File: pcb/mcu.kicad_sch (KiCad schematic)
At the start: 15 parts, among them J1 AVR-UPDI-6, U1 ATtiny1616-MNR

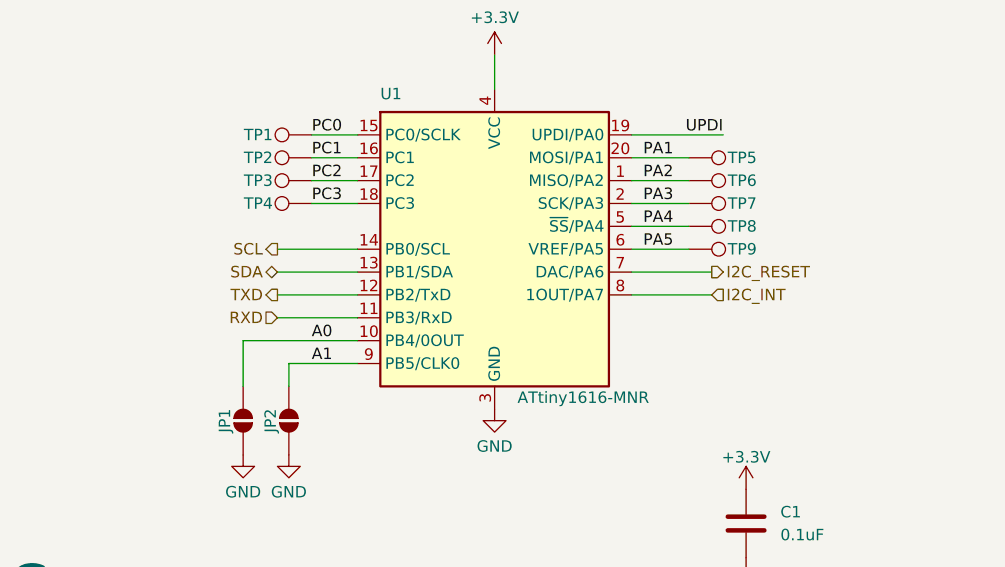
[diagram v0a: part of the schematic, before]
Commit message: Switched back to global lables
Updated all gnd and test point symbols
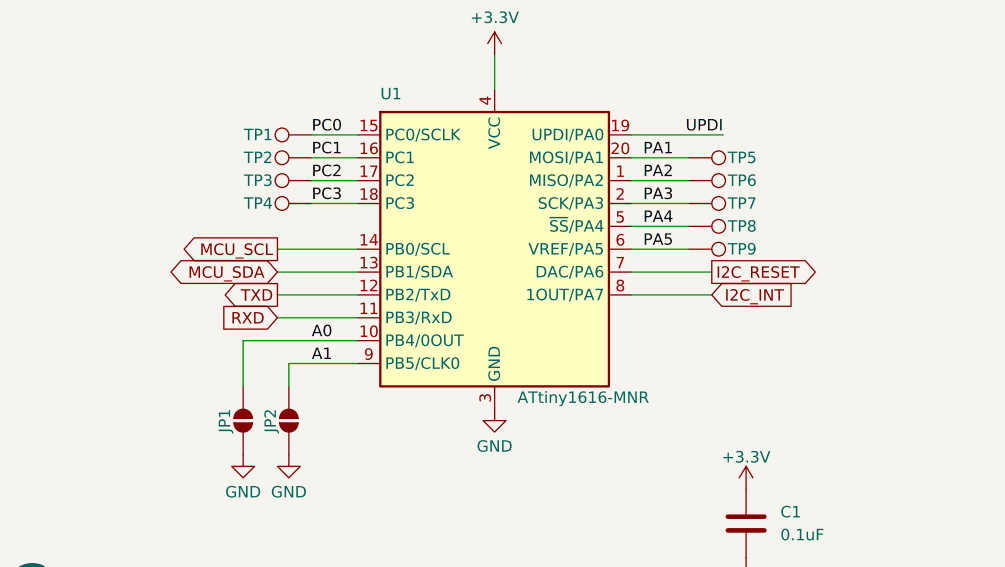
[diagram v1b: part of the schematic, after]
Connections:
- net SCL renamed MCU_SCL
- net SDA renamed MCU_SDA
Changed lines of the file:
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@@
 		)
 	)
-	(hierarchical_label "TXD"
-		(shape output)
-		(at 60.96 62.23 180)
+	(global_label "MCU_SDA"
+		(shape bidirectional)
+		(at 60.96 59.69 180)
+		(fields_autoplaced yes)
 		(effects
 			(font
@@
 			(justify right)
 		)
+		(property "Intersheetrefs" "${INTERSHEET_REFS}"
+			(at 48.2759 59.69 0)
+			(effects
+				(font
+					(size 1.27 1.27)
+				)
+				(justify right)
+			)
+		)
 	)
-	(hierarchical_label "SCL"
+	(global_label "TXD"
 		(shape output)
-		(at 60.96 57.15 180)
+		(at 60.96 62.23 180)
+		(fields_autoplaced yes)
 		(effects
 			(font
@@
 			(justify right)
 		)
+		(property "Intersheetrefs" "${INTERSHEET_REFS}"
+			(at 54.5277 62.23 0)
+			(effects
+				(font
+					(size 1.27 1.27)
+				)
+				(justify right)
+			)
+		)
 	)
-	(hierarchical_label "I2C_INT"
-		(shape input)
-		(at 109.22 62.23 0)
+	(global_label "MCU_SCL"
+		(shape output)
+		(at 60.96 57.15 180)
+		(fields_autoplaced yes)
+		(effects
+			(font
+				(size 1.27 1.27)
+			)
+			(justify right)
+		)
+		(property "Intersheetrefs" "${INTERSHEET_REFS}"
+			(at 49.4477 57.15 0)
+			(effects
+				(font
+					(size 1.27 1.27)
+				)
+				(justify right)
+			)
+		)
+	)
+	(global_label "I2C_RESET"
+		(shape output)
+		(at 109.22 59.69 0)
+		(fields_autoplaced yes)
 		(effects
 			(font
@@
 			(justify left)
 		)
+		(property "Intersheetrefs" "${INTERSHEET_REFS}"
+			(at 122.0022 59.69 0)
+			(effects
+				(font
+					(size 1.27 1.27)
+				)
+				(justify left)
+			)
+		)
 	)
-	(hierarchical_label "RXD"
+	(global_label "I2C_INT"
+		(shape input)
+		(at 109.22 62.23 0)
+		(fields_autoplaced yes)
+		(effects
+			(font
+				(size 1.27 1.27)
+			)
+			(justify left)
+		)
+		(property "Intersheetrefs" "${INTERSHEET_REFS}"
+			(at 119.16 62.23 0)
+			(effects
+				(font
+					(size 1.27 1.27)
+				)
+				(justify left)
+			)
+		)
+	)
+	(global_label "RXD"
 		(shape input)
 		(at 60.96 64.77 180)
+		(fields_autoplaced yes)
 		(effects
 			(font
@@
 			(justify right)
 		)
-	)
-	(hierarchical_label "SDA"
-		(shape bidirectional)
-		(at 60.96 59.69 180)
-		(effects
-			(font
-				(size 1.27 1.27)
+		(property "Intersheetrefs" "${INTERSHEET_REFS}"
+			(at 54.2253 64.77 0)
+			(effects
+				(font
+					(size 1.27 1.27)
+				)
+				(justify right)
 			)
-			(justify right)
 		)
 	)
-	(hierarchical_label "I2C_RESET"
-		(shape output)
-		(at 109.22 59.69 0)
-		(effects
-			(font
-				(size 1.27 1.27)
-			)
-			(justify left)
-		)
-	)
